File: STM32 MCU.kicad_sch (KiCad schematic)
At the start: 33 parts, among them J11 Conn_01x04_Socket, J4 Conn_01x04_Pin, J5 Conn_01x02_Pin, SW2 SW_Push, SW5 SW_Push, U3 STM32G474RETx, Y1 16MHz

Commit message: Schematic formating
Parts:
- removed J11: Conn_01x04_Socket, Connector_Molex:Molex_SL_171971-0004_1x04_P2.54mm_Vertical, symbol Connector:Conn_01x04_Socket
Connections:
- net USB-C_CC1 is gone; now on net MATRIX_R1: U3.59 (PB6)
- net USB-C_CC2 is gone; now on net MATRIX_C: U3.57 (PB4)
- net MATRIX_C: no longer U3.4 (PC15)
- net SPI1_MISO: now also R13.1, U3.20 (PA6)
- net SPI1_MOSI: now also R12.1, U3.21 (PA7)
- net SPI1_SCLK: now also R14.1, U3.19 (PA5)
- net 3V3_VOLTS: now reaches R15.2, U3.18 (PA4)
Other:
- note added: "3V3 BUS MONITOR"
- note added: "BOOT BUTTON"
- note added: "RESET BUTTON"
- note added: "SPI ZERO OHMS RES"
- note removed: "RESET AND BOOT BUTTONS"
- note removed: "SWD Connector"
- moved on the sheet: C1, C10, C11, C2, C3, C4, C42, C5, C6, C7, C8, C9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

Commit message: Schematic tiddy up
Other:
- title: (none) -> STM32G4 Schematic
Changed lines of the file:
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@@
 	(generator_version "10.0")
 	(paper "A4")
+	(title_block
+		(title "STM32G4 Schematic")
+		(rev "0")
+		(comment 1 "Xander Beal")
+	)
 	(rectangle
 		(start 152.4 19.05)

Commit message: small changes
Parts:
- J4: footprint Connector_PinHeader_2.54mm:PinHeader_1x04_P2.54mm_Vertical -> Connector_Molex:Molex_SL_171971-0004_1x04_P2.54mm_Vertical
- J5: footprint Connector_PinHeader_2.54mm:PinHeader_1x02_P2.54mm_Vertical -> Connector_Molex:Molex_SL_171971-0002_1x02_P2.54mm_Vertical
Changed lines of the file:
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@@
 			)
 		)
-		(property "Footprint" "Connector_PinHeader_2.54mm:PinHeader_1x04_P2.54mm_Vertical"
+		(property "Footprint" "Connector_Molex:Molex_SL_171971-0004_1x04_P2.54mm_Vertical"
 			(at 212.09 29.21 0)
 			(hide yes)
@@
 			)
 		)
-		(property "Footprint" "Connector_PinHeader_2.54mm:PinHeader_1x02_P2.54mm_Vertical"
+		(property "Footprint" "Connector_Molex:Molex_SL_171971-0002_1x02_P2.54mm_Vertical"
 			(at 212.09 41.91 0)
 			(hide yes)

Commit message: Final PCB from Xander
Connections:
- net BOOT0: now also J4.3 (Pin_3); no longer J4.2 (Pin_2)
- net SPI1_MISO: no longer R13.1, U3.20 (PA6)
- net SPI1_MOSI: no longer R12.1, U3.21 (PA7)
- net SPI1_SCLK: no longer R14.1, U3.19 (PA5)
- net SWDCLK: now also J4.2 (Pin_2); no longer J4.3 (Pin_3)
- net SWDIO: now also J4.1 (Pin_1); no longer J4.4 (Pin_4)
- net nRST: now also J4.4 (Pin_4); no longer J4.1 (Pin_1)
- new net SPI1_MISO_0: R13.1, U3.20 (PA6)
- new net SPI1_MOSI_0: R12.1, U3.21 (PA7)
- new net SPI1_SCLK_0: R14.1, U3.19 (PA5)
- no-connect marks 1 -> 3
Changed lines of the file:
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@@
 	)
 	(rectangle
-		(start 187.96 110.49)
-		(end 238.76 124.46)
+		(start 186.69 110.49)
+		(end 238.76 125.73)
 		(stroke
 			(width 0.254)
@@
 	)
 	(no_connect
+		(at 52.07 95.25)
+	)
+	(no_connect
+		(at 52.07 97.79)
+	)
+	(no_connect
 		(at 52.07 54.61)
 	)
@@
 	(wire
 		(pts
-			(xy 189.23 118.11) (xy 208.28 118.11)
+			(xy 187.96 118.11) (xy 208.28 118.11)
 		)
 		(stroke
@@
 	(wire
 		(pts
+			(xy 187.96 26.67) (xy 207.01 26.67)
+		)
+		(stroke
+			(width 0)
+			(type default)
+		)
+	)
+	(wire
+		(pts
 			(xy 87.63 118.11) (xy 107.95 118.11)
 		)
@@
 	(wire
 		(pts
-			(xy 189.23 121.92) (xy 200.66 121.92)
+			(xy 187.96 121.92) (xy 200.66 121.92)
 		)
 		(stroke
@@
 	(wire
 		(pts
-			(xy 186.69 31.75) (xy 207.01 31.75)
-		)
-		(stroke
-			(width 0)
-			(type default)
-		)
-	)
-	(wire
-		(pts
 			(xy 165.1 34.29) (xy 165.1 36.83)
 		)
@@
 	(wire
 		(pts
-			(xy 186.69 26.67) (xy 207.01 26.67)
-		)
-		(stroke
-			(width 0)
-			(type default)
-		)
-	)
-	(wire
-		(pts
 			(xy 87.63 80.01) (xy 107.95 80.01)
 		)
@@
 	(wire
 		(pts
+			(xy 187.96 31.75) (xy 207.01 31.75)
+		)
+		(stroke
+			(width 0)
+			(type default)
+		)
+	)
+	(wire
+		(pts
 			(xy 87.63 54.61) (xy 107.95 54.61)
 		)
@@
 	(wire
 		(pts
+			(xy 187.96 29.21) (xy 207.01 29.21)
+		)
+		(stroke
+			(width 0)
+			(type default)
+		)
+	)
+	(wire
+		(pts
 			(xy 215.9 118.11) (xy 226.06 118.11)
 		)
@@
 	(wire
 		(pts
-			(xy 189.23 114.3) (xy 215.9 114.3)
+			(xy 187.96 114.3) (xy 215.9 114.3)
 		)
 		(stroke
@@
 	(wire
 		(pts
+			(xy 187.96 24.13) (xy 207.01 24.13)
+		)
+		(stroke
+			(width 0)
+			(type default)
+		)
+	)
+	(wire
+		(pts
 			(xy 87.63 107.95) (xy 107.95 107.95)
 		)
@@
 	(wire
 		(pts
-			(xy 186.69 24.13) (xy 207.01 24.13)
-		)
-		(stroke
-			(width 0)
-			(type default)
-		)
-	)
-	(wire
-		(pts
 			(xy 53.34 170.18) (xy 53.34 171.45)
 		)
@@
 	(wire
 		(pts
-			(xy 186.69 29.21) (xy 207.01 29.21)
-		)
-		(stroke
-			(width 0)
-			(type default)
-		)
-	)
-	(wire
-		(pts
 			(xy 31.75 85.09) (xy 52.07 85.09)
 		)
@@
 		)
 	)
-	(label "SPI1_MISO"
-		(at 189.23 118.11 0)
+	(label "SPI1_MOSI_0"
+		(at 107.95 54.61 180)
+		(effects
+			(font
+				(size 1.27 1.27)
+			)
+			(justify right bottom)
+		)
+	)
+	(label "SPI1_MISO_0"
+		(at 187.96 118.11 0)
 		(effects
 			(font
@@
 		)
 	)
-	(label "SPI1_SCLK"
-		(at 189.23 114.3 0)
+	(label "SPI1_SCLK_0"
+		(at 187.96 114.3 0)
 		(effects
 			(font
@@
 			)
 			(justify left bottom)
-		)
-	)
-	(label "SPI1_MISO"
-		(at 107.95 52.07 180)
-		(effects
-			(font
-				(size 1.27 1.27)
-			)
-			(justify right bottom)
 		)
 	)
@@
 	)
 	(label "nRST"
-		(at 186.69 31.75 0)
+		(at 187.96 24.13 0)
 		(effects
 			(font
@@
 			)
 			(justify left bottom)
+		)
+	)
+	(label "SPI1_SCLK_0"
+		(at 107.95 49.53 180)
+		(effects
+			(font
+				(size 1.27 1.27)
+			)
+			(justify right bottom)
 		)
 	)
@@
 	)
 	(label "SWDIO"
-		(at 186.69 24.13 0)
+		(at 187.96 31.75 0)
 		(effects
 			(font
@@
 			)
 			(justify left bottom)
-		)
-	)
-	(label "SPI1_SCLK"
-		(at 107.95 49.53 180)
-		(effects
-			(font
-				(size 1.27 1.27)
-			)
-			(justify right bottom)
 		)
 	)
@@
 		)
 	)
-	(label "SPI1_MOSI"
-		(at 189.23 121.92 0)
+	(label "SPI1_MOSI_0"
+		(at 187.96 121.92 0)
 		(effects
 			(font
@@
 		)
 	)
+	(label "SPI1_MISO_0"
+		(at 107.95 52.07 180)
+		(effects
+			(font
+				(size 1.27 1.27)
+			)
+			(justify right bottom)
+		)
+	)
 	(label "BOOT0"
-		(at 186.69 29.21 0)
+		(at 187.96 26.67 0)
 		(effects
 			(font
@@
 	)
 	(label "SWDCLK"
-		(at 186.69 26.67 0)
+		(at 187.96 29.21 0)
 		(effects
 			(font
@@
 		(effects
 			(font
-				(size 1.27 1.27)
-			)
-			(justify right bottom)
-		)
-	)
-	(label "SPI1_MOSI"
-		(at 107.95 54.61 180)
-		(effects
-			(font

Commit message: moving usbc to power section, added poewr delivery IC
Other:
- note added: "pa10 - usbpd dbcc2 pa9 - usbpd dbcc1"
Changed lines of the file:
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@@
+		)
+	)
+	(text "pa10 - usbpd dbcc2\npa9 - usbpd dbcc1"
+		(exclude_from_sim no)
+		(at 129.794 51.054 0)
+		(effects
+			(font
+				(size 1.27 1.27)
+			)
 		)
 	)

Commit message: changed vbus
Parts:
- R10: value 10k -> 3.3
- R9: value 7k -> 17
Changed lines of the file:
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@@
 		)
 	)
-	(text_box "USB Spec 4.5V - 5.5V"
+	(text_box "USB Spec 20V"
 		(exclude_from_sim no)
 		(at 190.5 87.9871 0)
@@
 			)
 		)
-		(property "Value" "10k"
+		(property "Value" "3.3"
 			(at 210.82 85.344 0)
 			(show_name no)
@@
 			)
 		)
-		(property "Value" "7k"
+		(property "Value" "17"
 			(at 210.82 75.438 0)
 			(show_name no)

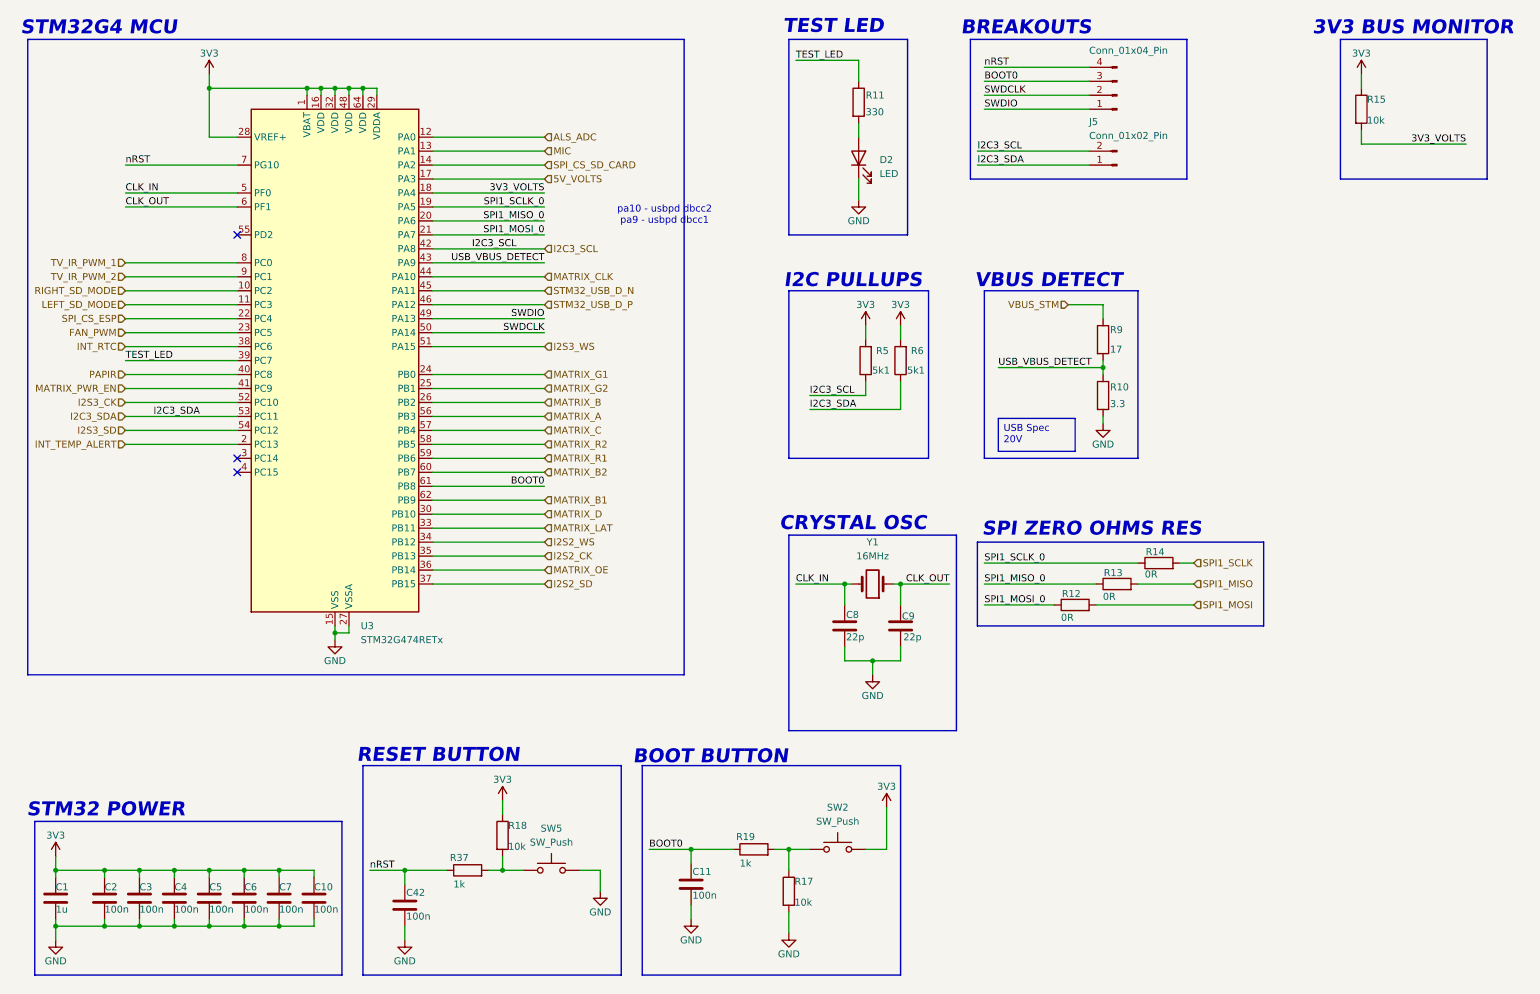
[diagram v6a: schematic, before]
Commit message: adding cc pins to stm32g4
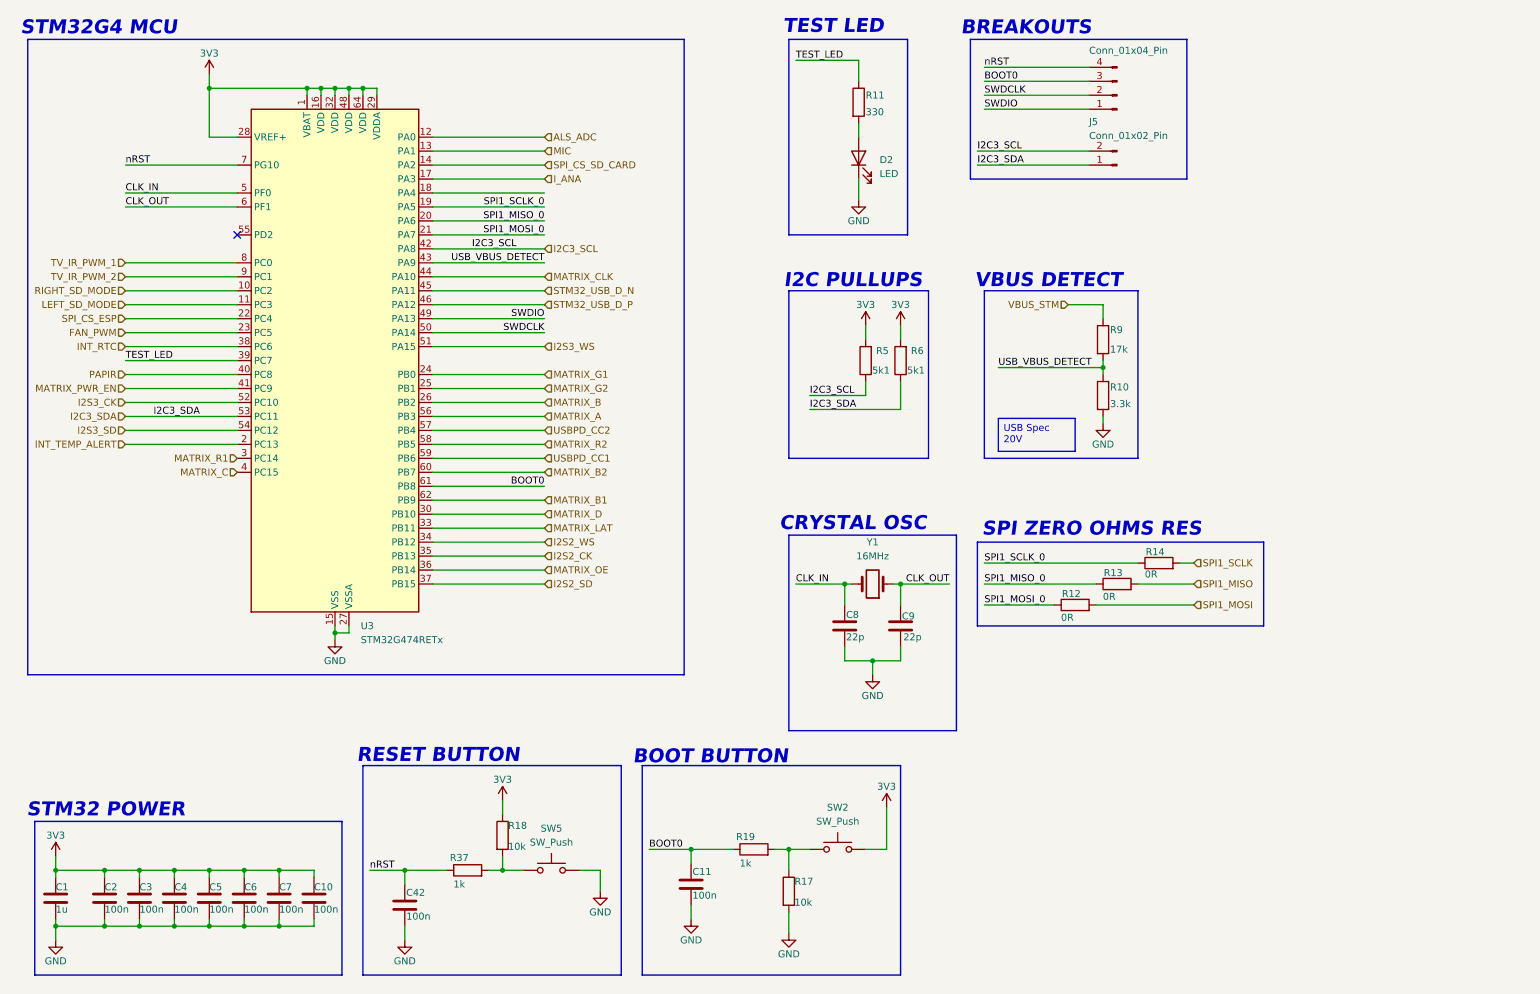
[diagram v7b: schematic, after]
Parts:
- removed R15: 10k, Resistor_SMD:R_0603_1608Metric, symbol Device:R
- R10: value 3.3 -> 3.3k
- R9: value 17 -> 17k
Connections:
- net MATRIX_C: now also U3.4 (PC15); no longer U3.57 (PB4)
- net MATRIX_R1: now also U3.3 (PC14); no longer U3.59 (PB6)
- net 3V3_VOLTS: no longer names the net of U3.18 (PA4)
- net 5V_VOLTS renamed I_ANA
- new net USBPD_CC1: U3.59 (PB6)
- new net USBPD_CC2: U3.57 (PB4)
- no-connect marks 3 -> 1
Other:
- note removed: "3V3 BUS MONITOR"
- note removed: "pa10 - usbpd dbcc2 pa9 - usbpd dbcc1"
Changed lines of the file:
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@@
 		)
 	)
-	(rectangle
-		(start 252.73 19.05)
-		(end 279.4 44.45)
-		(stroke
-			(width 0.254)
-			(type solid)
-		)
-		(fill
-			(type none)
-		)
-	)
 	(text "I2C PULLUPS\n"
 		(exclude_from_sim no)
@@
 		)
 	)
-	(text "pa10 - usbpd dbcc2\npa9 - usbpd dbcc1"
-		(exclude_from_sim no)
-		(at 129.794 51.054 0)
-		(effects
-			(font
-				(size 1.27 1.27)
-			)
-		)
-	)
 	(text "SPI ZERO OHMS RES"
 		(exclude_from_sim no)
@@
 		)
 	)
-	(text "3V3 BUS MONITOR"
-		(exclude_from_sim no)
-		(at 265.938 17.018 0)
-		(effects
-			(font
-				(size 2.54 2.54)
-				(thickness 0.508)
-				(bold yes)
-				(italic yes)
-				(color 0 0 194 1)
-			)
-		)
-	)
 	(text "STM32G4 MCU"
 		(exclude_from_sim no)
@@
 	)
 	(no_connect
-		(at 52.07 95.25)
-	)
-	(no_connect
-		(at 52.07 97.79)
-	)
-	(no_connect
 		(at 52.07 54.61)
 	)
@@
 	(wire
 		(pts
-			(xy 256.54 25.4) (xy 256.54 27.94)
-		)
-		(stroke
-			(width 0)
-			(type default)
-		)
-	)
-	(wire
-		(pts
 			(xy 46.99 27.94) (xy 64.77 27.94)
 		)
@@
 	(wire
 		(pts
-			(xy 275.59 38.1) (xy 256.54 38.1)
-		)
-		(stroke
-			(width 0)
-			(type default)
-		)
-	)
-	(wire
-		(pts
 			(xy 170.18 158.75) (xy 170.18 166.37)
 		)
@@
 	(wire
 		(pts
-			(xy 256.54 38.1) (xy 256.54 35.56)
-		)
-		(stroke
-			(width 0)
-			(type default)
-		)
-	)
-	(wire
-		(pts
 			(xy 87.63 92.71) (xy 107.95 92.71)
 		)
@@
 		)
 	)
-	(label "3V3_VOLTS"
-		(at 275.59 38.1 180)
-		(effects
-			(font
-				(size 1.27 1.27)
-			)
-			(justify right bottom)
-		)
-	)
 	(label "nRST"
 		(at 31.75 41.91 0)
@@
 		)
 	)
-	(label "3V3_VOLTS"
-		(at 107.95 46.99 180)
-		(effects
-			(font
-				(size 1.27 1.27)
-			)
-			(justify right bottom)
-		)
-	)
 	(label "CLK_IN"
 		(at 153.67 118.11 0)
@@
 		)
 	)
-	(hierarchical_label "5V_VOLTS"
+	(hierarchical_label "I_ANA"
 		(shape input)
 		(at 107.95 44.45 0)
@@
 		)
 	)
+	(hierarchical_label "USBPD_CC1"
+		(shape input)
+		(at 107.95 95.25 0)
+		(effects
+			(font
+				(size 1.27 1.27)
+			)
+			(justify left)
+		)
+	)
 	(hierarchical_label "SPI_CS_SD_CARD"
 		(shape input)
@@
 		)
 	)
+	(hierarchical_label "MATRIX_C"
+		(shape input)
+		(at 52.07 97.79 180)
+		(effects
+			(font
+				(size 1.27 1.27)
+			)
+			(justify right)
+		)
+	)
 	(hierarchical_label "MATRIX_CLK"
 		(shape input)
@@
 		)
 	)
+	(hierarchical_label "MATRIX_R1"
+		(shape input)
+		(at 52.07 95.25 180)
+		(effects
+			(font
+				(size 1.27 1.27)
+			)
+			(justify right)
+		)
+	)
 	(hierarchical_label "INT_RTC"
 		(shape input)
@@
 		)
 	)
-	(hierarchical_label "I2S3_WS"
+	(hierarchical_label "USBPD_CC2"
 		(shape input)
-		(at 107.95 74.93 0)
+		(at 107.95 90.17 0)
 		(effects
 			(font
@@
 		)
 	)
-	(hierarchical_label "MATRIX_R1"
+	(hierarchical_label "I2S3_WS"
 		(shape input)
-		(at 107.95 95.25 0)
+		(at 107.95 74.93 0)
 		(effects
 			(font
@@
 		)
 	)
-	(hierarchical_label "MATRIX_C"
-		(shape input)
-		(at 107.95 90.17 0)
-		(effects
-			(font
-				(size 1.27 1.27)
-			)
-			(justify left)
-		)
-	)
 	(hierarchical_label "MATRIX_B1"
 		(shape input)
@@
 			)
 		)
-		(property "Value" "3.3"
+		(property "Value" "3.3k"
 			(at 210.82 85.344 0)
 			(show_name no)
@@
 	(symbol
 		(lib_id "Device:R")
-		(at 256.54 31.75 0)
-		(unit 1)
-		(body_style 1)
-		(exclude_from_sim no)
-		(in_bom yes)
-		(on_board yes)
-		(in_pos_files yes)
-		(dnp no)
-		(property "Reference" "R15"
-			(at 257.556 29.972 0)
-			(show_name no)
-			(do_not_autoplace no)
-			(effects
-				(font
-					(size 1.27 1.27)
-				)
-				(justify left)
-			)
-		)
-		(property "Value" "10k"
-			(at 257.556 33.782 0)
-			(show_name no)
-			(do_not_autoplace no)
-			(effects
-				(font
-					(size 1.27 1.27)
-				)
-				(justify left)
-			)
-		)
-		(property "Footprint" "Resistor_SMD:R_0603_1608Metric"
-			(at 254.762 31.75 90)
-			(hide yes)
-			(show_name no)
-			(do_not_autoplace no)
-			(effects
-				(font
-					(size 1.27 1.27)
-				)
-			)
-		)
-		(property "Datasheet" ""
-			(at 256.54 31.75 0)
-			(hide yes)
-			(show_name no)
-			(do_not_autoplace no)
-			(effects
-				(font
-					(size 1.27 1.27)
-				)
-			)
-		)
-		(property "Description" "Resistor"
-			(at 256.54 31.75 0)
-			(hide yes)
-			(show_name no)
-			(do_not_autoplace no)
-			(effects
-				(font
-					(size 1.27 1.27)
-				)
-			)
-		)
-		(pin "1"
-		)
-		(pin "2"
-		)
-		(instances
-			(project "SeniorDesign_PCB"
-				(path "/88e1ced0-9576-4565-ab29-f74bf51ccbda/27166b61-357c-42c1-9fa2-b71231f12fe0"
-					(reference "R15")
-					(unit 1)
-				)
-			)
-		)
-	)
-	(symbol
-		(lib_id "Device:R")
 		(at 166.37 77.47 180)
 		(unit 1)
@@
 	)
 	(symbol
-		(lib_id "power:+3V3")
-		(at 256.54 25.4 0)
-		(unit 1)
-		(body_style 1)
-		(exclude_from_sim no)
-		(in_bom yes)
-		(on_board yes)
-		(in_pos_files yes)
-		(dnp no)
-		(property "Reference" "#PWR0136"
-			(at 256.54 29.21 0)
-			(hide yes)
-			(show_name no)
-			(do_not_autoplace no)
-			(effects
-				(font
-					(size 1.27 1.27)
-				)
-			)
-		)
-		(property "Value" "3V3"
-			(at 256.54 21.59 0)
-			(show_name no)
-			(do_not_autoplace no)
-			(effects
-				(font
-					(size 1.27 1.27)
-				)
-			)
-		)
-		(property "Footprint" ""
-			(at 256.54 25.4 0)
-			(hide yes)
-			(show_name no)
-			(do_not_autoplace no)
-			(effects
-				(font
-					(size 1.27 1.27)
-				)
-			)
-		)
-		(property "Datasheet" ""
-			(at 256.54 25.4 0)
-			(hide yes)
-			(show_name no)
-			(do_not_autoplace no)
-			(effects
-				(font
-					(size 1.27 1.27)
-				)
-			)
-		)
-		(property "Description" "Power symbol creates a global label with name \"+3V3\""
-			(at 256.54 25.4 0)
-			(hide yes)
-			(show_name no)
-			(do_not_autoplace no)
-			(effects
-				(font
-					(size 1.27 1.27)
-				)
-			)
-		)
-		(pin "1"
-		)
-		(instances
-			(project "SeniorDesign_PCB"
-				(path "/88e1ced0-9576-4565-ab29-f74bf51ccbda/27166b61-357c-42c1-9fa2-b71231f12fe0"
-					(reference "#PWR0136")
-					(unit 1)
-				)
-			)
-		)
-	)
-	(symbol
 		(lib_id "Device:R")
 		(at 219.71 114.3 90)
@@
 			)
 		)
-		(property "Value" "17"
+		(property "Value" "17k"
 			(at 210.82 75.438 0)
 			(show_name no)
